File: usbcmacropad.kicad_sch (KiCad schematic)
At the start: 6 parts, among them SW1 SW_Push, SW2 SW_Push, SW3 SW_Push, SW4 SW_Push, U1 XIAO-RP2040-DIP

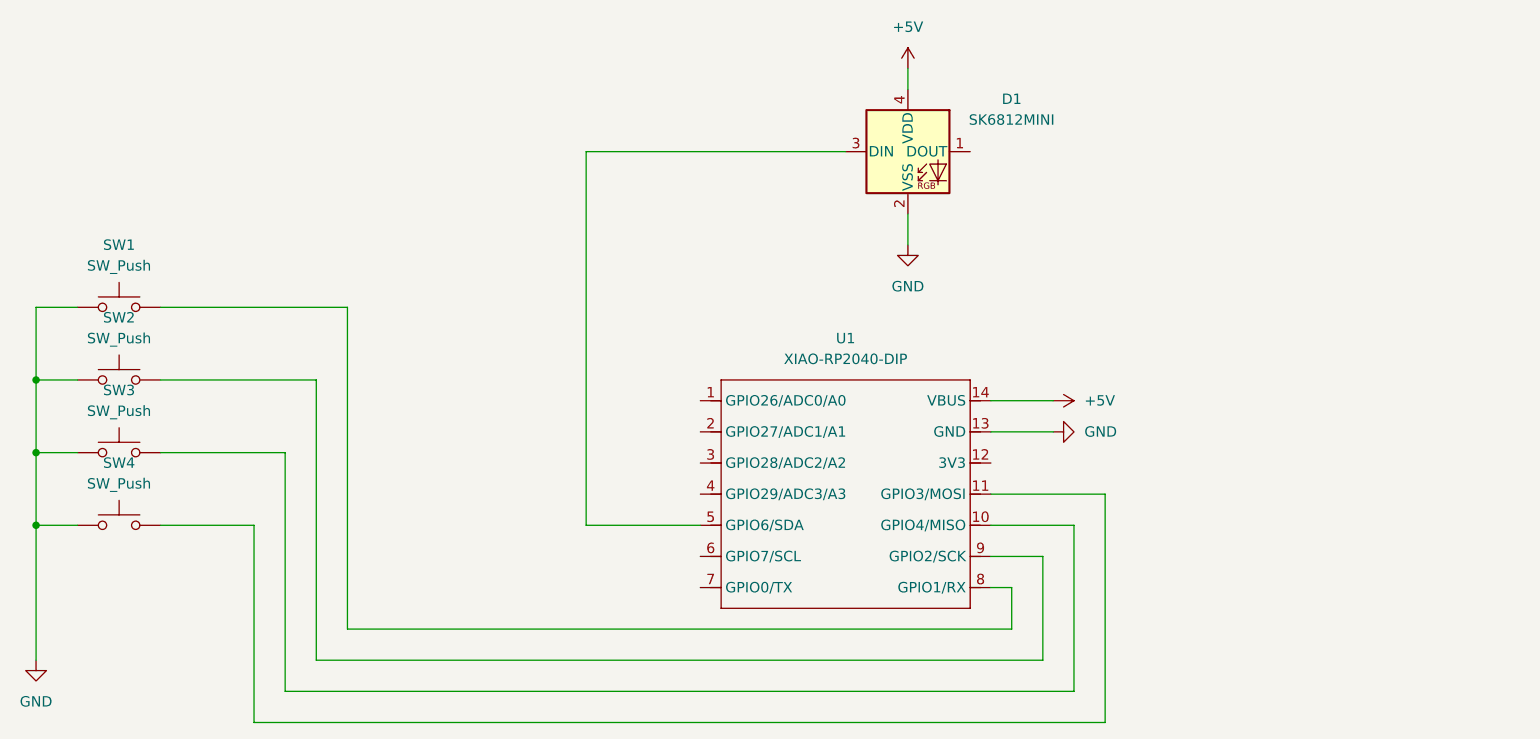
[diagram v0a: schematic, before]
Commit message: Added OLED Display and edited connections
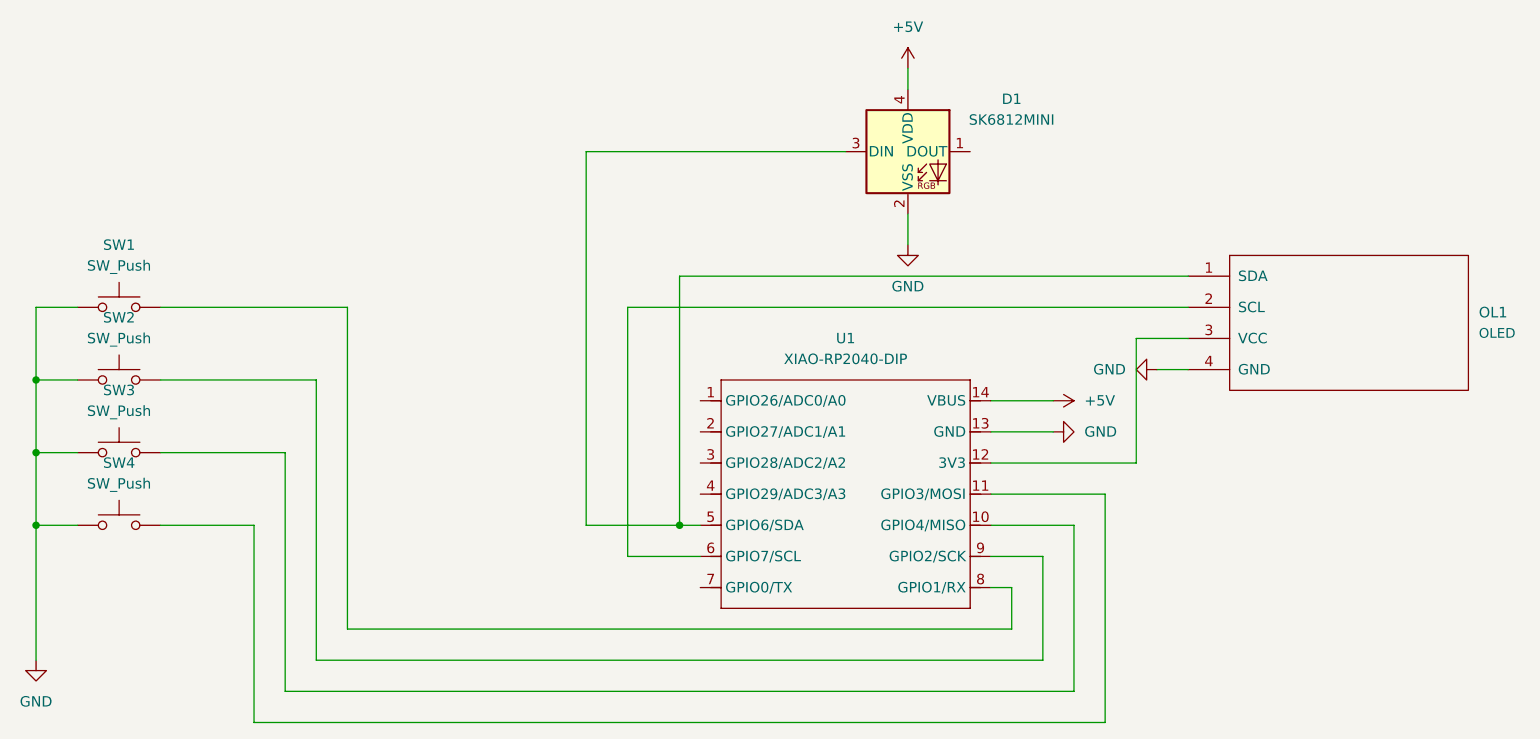
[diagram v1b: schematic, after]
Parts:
- added OL1: OLED, oled:SSD1306-0.91-OLED-4pin-128x32, symbol kbd:OLED
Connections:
- net GND: now also OL1.4 (GND)
- net at D1.3 (DIN), U1.5 (GPIO6/SDA): now also OL1.1 (SDA)
- net at U1.12 (3V3): now also OL1.3 (VCC)
- net at U1.6 (GPIO7/SCL): now also OL1.2 (SCL)
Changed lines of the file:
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@@
 		(color 0 0 0 0)
 	)
+	(junction
+		(at 114.3 85.09)
+		(diameter 0)
+		(color 0 0 0 0)
+	)
 	(wire
 		(pts
@@
 	(wire
 		(pts
+			(xy 170.18 77.47) (xy 152.4 77.47)
+		)
+		(stroke
+			(width 0)
+			(type default)
+		)
+	)
+	(wire
+		(pts
 			(xy 152.4 85.09) (xy 162.56 85.09)
 		)
@@
 	(wire
 		(pts
+			(xy 176.53 62.23) (xy 170.18 62.23)
+		)
+		(stroke
+			(width 0)
+			(type default)
+		)
+	)
+	(wire
+		(pts
 			(xy 73.66 58.42) (xy 73.66 97.79)
 		)
@@
 	(wire
 		(pts
+			(xy 107.95 58.42) (xy 107.95 88.9)
+		)
+		(stroke
+			(width 0)
+			(type default)
+		)
+	)
+	(wire
+		(pts
+			(xy 114.3 54.61) (xy 114.3 85.09)
+		)
+		(stroke
+			(width 0)
+			(type default)
+		)
+	)
+	(wire
+		(pts
 			(xy 50.8 85.09) (xy 62.23 85.09)
 		)
@@
 	(wire
 		(pts
+			(xy 176.53 54.61) (xy 114.3 54.61)
+		)
+		(stroke
+			(width 0)
+			(type default)
+		)
+	)
+	(wire
+		(pts
 			(xy 35.56 85.09) (xy 40.64 85.09)
 		)
@@
 	(wire
 		(pts
-			(xy 102.87 85.09) (xy 116.84 85.09)
+			(xy 102.87 85.09) (xy 114.3 85.09)
 		)
 		(stroke
@@
 	(wire
 		(pts
+			(xy 107.95 88.9) (xy 116.84 88.9)
+		)
+		(stroke
+			(width 0)
+			(type default)
+		)
+	)
+	(wire
+		(pts
 			(xy 142.24 46.99) (xy 142.24 50.8)
 		)
@@
 	(wire
 		(pts
+			(xy 172.72 66.04) (xy 176.53 66.04)
+		)
+		(stroke
+			(width 0)
+			(type default)
+		)
+	)
+	(wire
+		(pts
 			(xy 160.02 69.85) (xy 152.4 69.85)
 		)
@@
 	(wire
 		(pts
+			(xy 170.18 62.23) (xy 170.18 77.47)
+		)
+		(stroke
+			(width 0)
+			(type default)
+		)
+	)
+	(wire
+		(pts
+			(xy 114.3 85.09) (xy 116.84 85.09)
+		)
+		(stroke
+			(width 0)
+			(type default)
+		)
+	)
+	(wire
+		(pts
 			(xy 158.75 88.9) (xy 158.75 101.6)
 		)
@@
 		(pts
 			(xy 166.37 109.22) (xy 166.37 81.28)
+		)
+		(stroke
+			(width 0)
+			(type default)
+		)
+	)
+	(wire
+		(pts
+			(xy 176.53 58.42) (xy 107.95 58.42)
 		)
 		(stroke
@@
 	(symbol
 		(lib_id "power:GND")
+		(at 172.72 66.04 270)
+		(unit 1)
+		(exclude_from_sim no)
+		(in_bom yes)
+		(on_board yes)
+		(dnp no)
+		(fields_autoplaced yes)
+		(property "Reference" "#PWR06"
+			(at 166.37 66.04 0)
+			(effects
+				(font
+					(size 1.27 1.27)
+				)
+				(hide yes)
+			)
+		)
+		(property "Value" "GND"
+			(at 168.91 66.0399 90)
+			(effects
+				(font
+					(size 1.27 1.27)
+				)
+				(justify right)
+			)
+		)
+		(property "Footprint" ""
+			(at 172.72 66.04 0)
+			(effects
+				(font
+					(size 1.27 1.27)
+				)
+				(hide yes)
+			)
+		)
+		(property "Datasheet" ""
+			(at 172.72 66.04 0)
+			(effects
+				(font
+					(size 1.27 1.27)
+				)
+				(hide yes)
+			)
+		)
+		(property "Description" "Power symbol creates a global label with name \"GND\" , ground"
+			(at 172.72 66.04 0)
+			(effects
+				(font
+					(size 1.27 1.27)
+				)
+				(hide yes)
+			)
+		)
+		(pin "1"
+		)
+		(instances
+			(project ""
+				(path "/9f447f21-215d-459c-ab64-0873cc520878"
+					(reference "#PWR06")
+					(unit 1)
+				)
+			)
+		)
+	)
+	(symbol
+		(lib_id "power:GND")
 		(at 160.02 73.66 90)
 		(unit 1)
@@
 					(unit 1)
 				)
+			)
+		)
+	)
+	(symbol
+		(lib_id "kbd:OLED")
+		(at 195.58 60.96 0)
+		(unit 1)
+		(exclude_from_sim no)
+		(in_bom yes)
+		(on_board yes)
+		(dnp no)
+		(fields_autoplaced yes)
+		(property "Reference" "OL1"
+			(at 212.09 59.055 0)
+			(effects
+				(font
+					(size 1.2954 1.2954)
+				)
+				(justify left)
+			)
+		)
+		(property "Value" "OLED"
+			(at 212.09 61.595 0)
+			(effects
+				(font
+					(size 1.1938 1.1938)
+				)
+				(justify left)
+			)
+		)
+		(property "Footprint" "oled:SSD1306-0.91-OLED-4pin-128x32"
+			(at 195.58 58.42 0)
+			(effects
+				(font
+					(size 1.524 1.524)
+				)
+				(hide yes)
+			)
+		)
+		(property "Datasheet" ""
+			(at 195.58 58.42 0)
+			(effects
+				(font
+					(size 1.524 1.524)
+				)
+				(hide yes)
+			)
+		)
+		(property "Description" ""
+			(at 195.58 60.96 0)
+			(effects
+				(font
+					(size 1.27 1.27)
+				)
+				(hide yes)
+			)
+		)
+		(pin "1"
+		)
+		(pin "2"
+		)
+		(pin "3"
+		)
+		(pin "4"
+		)
+		(instances
+			(project ""
+				(path "/9f447f21-215d-459c-ab64-0873cc520878"
+					(reference "OL1")
+					(unit 1)
+				)
